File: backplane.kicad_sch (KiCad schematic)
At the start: 9 parts, among them J0 212520-1006, J5 XT60PW-F

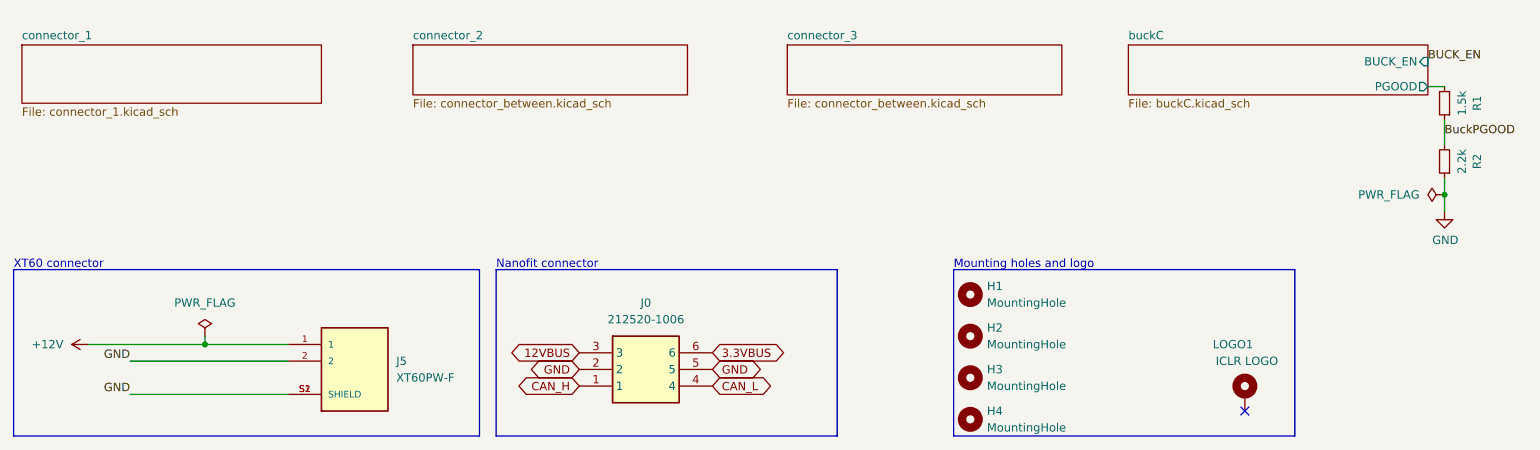
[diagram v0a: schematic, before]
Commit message: Overhaul of design
Changed out the SFMC Oresat connectors for the 46010-0622 Molex; added the SC4215; reduced from 4 connectors to three connectors - no changes made to the footprint, changes only made to the schematic for checks
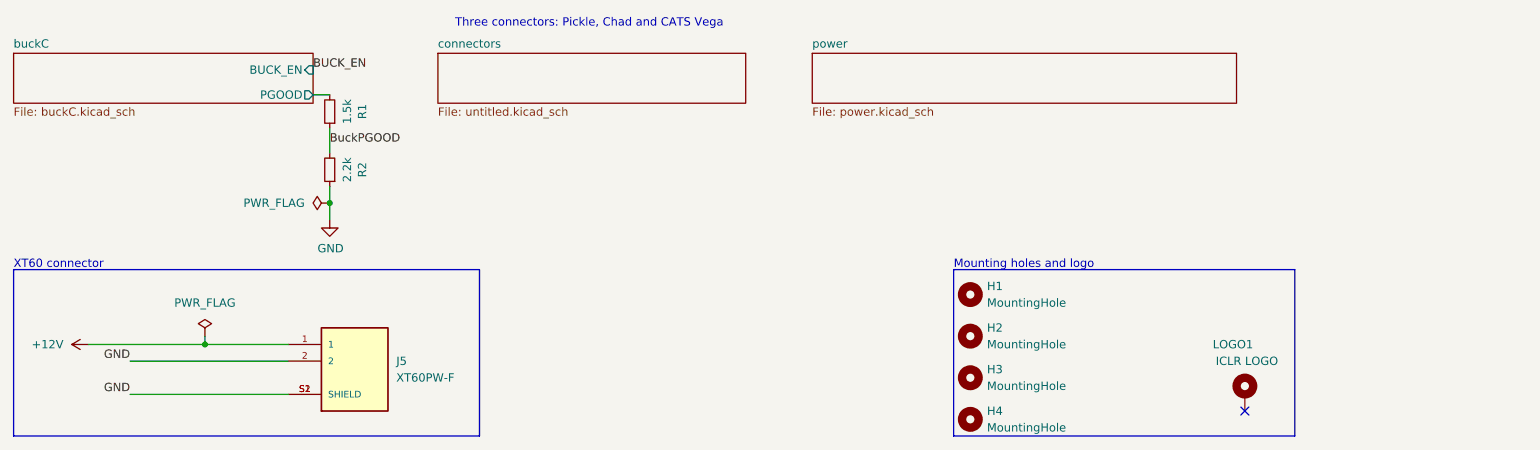
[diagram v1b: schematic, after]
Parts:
- removed J0: 212520-1006, Molex 212520-1006:212520-1006, symbol 212520-1006:212520-1006
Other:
- removed sheet connector_1
- removed sheet connector_2
- removed sheet connector_3
- added sheet connectors (untitled.kicad_sch)
- added sheet power (power.kicad_sch)
- note added: "Three connectors: Pickle, Chad and CATS Vega"
- note removed: "Nanofit connector"
- moved on the sheet: R1, R2
